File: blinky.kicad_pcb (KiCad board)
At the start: 4 copper layers, 50 x 50 mm, 118 parts, among them J1 Power, J3 Skedd, U1 STM32G030C6Tx, U2 BQ25570

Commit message: Sorting out DRC.
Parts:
- removed R72: 100, Resistor_SMD:R_0402_1005Metric
- removed the TP1 at (114.5, 44.5)
- removed the TP2 at (48.1, 89.2)
- added C20: 100u, Capacitor_SMD:C_1206_3216Metric, F.Cu at (117.5, 122.0)
- added C21: 100u, Capacitor_SMD:C_1206_3216Metric, F.Cu at (110.5, 122.0)
- added C22: 100u, Capacitor_SMD:C_1206_3216Metric, F.Cu at (103.5, 122.0)
- added C23: 100u, Capacitor_SMD:C_1206_3216Metric, F.Cu at (96.5, 122.0)
- added C24: 100u, Capacitor_SMD:C_1206_3216Metric, F.Cu at (89.5, 122.0)
- added C25: 100u, Capacitor_SMD:C_1206_3216Metric, F.Cu at (82.5, 122.0)
- moved TP2 23.7 mm to (93.0, 76.5)
- moved TP1 23.3 mm to (86.0, 79.5)
- moved TP3 20.2 mm to (86.0, 76.5)
- moved R27 5.98 mm to (105.8, 96.0), turned to -90 degrees
- moved R34 1.30 mm to (103.7, 95.2), turned to 90 degrees
- moved R33 1.22 mm to (95.9, 95.8)
- moved R44 1.03 mm to (103.7, 104.8), turned to -90 degrees
- moved R43 1.03 mm to (95.8, 104.3)
- moved C8 0.67 mm to (92.8, 101.2), turned to 90 degrees
- moved C1 0.25 mm to (94.3, 100.0)
- moved R21 0.13 mm to (85.5, 89.5)
- turned R24 to 180 degrees
- turned R45 to 180 degrees
- renumbered J3 to J2, R71 to R10, R73 to R18, R18 to R19, R19 to R20, R74 to R27, TP3 to TP1, TP4 to TP2, TP5 to TP3
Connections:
- J2 pad 1: /d3V3 -> +3V3
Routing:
- net +3V3: track 186.1 -> 273.0 mm, vias 0 -> 6
- net /VBatt: track 69.6 -> 141.6 mm
- net GND: track 16.1 -> 54.6 mm, vias 12 -> 34
- net Net-(D43-K): track 0.00 -> 2.73 mm, vias 0 -> 1
- net Net-(D33-K): track 0.00 -> 2.28 mm, vias 0 -> 1
- net /A15: track 0.00 -> 1.92 mm
- net /Vin: track 9.57 -> 11.5 mm
- net Net-(D44-K): track 0.00 -> 1.92 mm, vias 0 -> 1
- net Net-(D34-K): track 0.00 -> 1.91 mm, vias 0 -> 1
- net /A2: track 2.57 -> 0.75 mm
- net Net-(D66-K): track 0.00 -> 1.57 mm, vias 0 -> 1
- net Net-(D65-K): track 0.00 -> 1.57 mm, vias 0 -> 1
- net Net-(D64-K): track 0.00 -> 1.57 mm, vias 0 -> 1
- net Net-(D63-K): track 0.00 -> 1.57 mm, vias 0 -> 1
- net Net-(D62-K): track 0.00 -> 1.57 mm, vias 0 -> 1
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- added copper zone on B.Cu, net +3V3
- added copper zone on B.Cu, net GND
- added copper zone on In1.Cu, net GND
- added copper zone on In2.Cu, net GND

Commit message: Cap to the max.
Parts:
- added C10: 100u, Capacitor_SMD:C_1206_3216Metric, F.Cu at (78.8, 78.8)
- added C17: 100u, Capacitor_SMD:C_1206_3216Metric, F.Cu at (121.2, 78.8)
- added C22: 100u, Capacitor_SMD:C_1206_3216Metric, F.Cu at (121.2, 121.2)
- added C29: 100u, Capacitor_SMD:C_1206_3216Metric, F.Cu at (78.8, 121.2)
- added C9: 47u, Capacitor_SMD:C_0805_2012Metric, F.Cu at (91.7, 100.0)
- moved J1 1.13 mm to (79.9, 85.5), turned to -90 degrees
- moved C11 1.00 mm to (83.5, 78.0)
- moved C16 1.00 mm to (116.5, 78.0)
- moved C18 1.00 mm to (122.0, 83.5)
- moved C21 1.00 mm to (122.0, 116.5)
- moved C23 1.00 mm to (116.5, 122.0)
- moved C28 1.00 mm to (83.5, 122.0)
- moved C8 0.72 mm to (93.5, 101.7), turned to 180 degrees
- renumbered C10 to C11, C11 to C12, C12 to C13, C13 to C14, C14 to C15, C15 to C16, C16 to C18, C17 to C19, C18 to C20, C19 to C21, C20 to C23, C21 to C24, C22 to C25, C23 to C26, C24 to C27, C25 to C28
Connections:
- U1 pad 4: +3V3 -> Net-(U1-VBAT)
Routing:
- net GND: track 54.6 -> 61.1 mm, vias 34 -> 40
- net /VBatt: track 141.6 -> 147.5 mm
- net Net-(U1-VBAT): track 0.00 -> 3.97 mm
- net /RESET: track 27.1 -> 25.0 mm
- net +3V3: track 273.0 -> 271.4 mm, vias 6 -> 10
- net /Vin: track 11.5 -> 10.5 mm

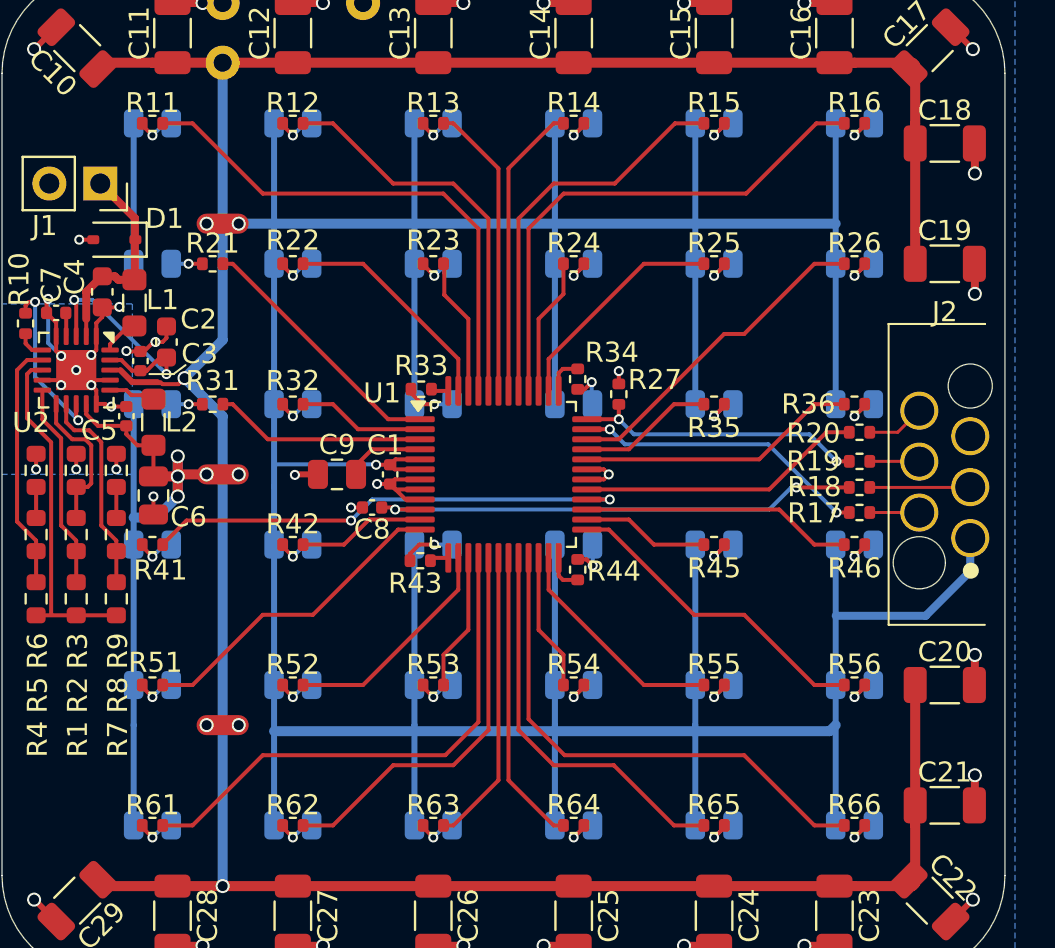
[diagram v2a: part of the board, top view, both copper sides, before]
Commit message: Sort out resistor values.
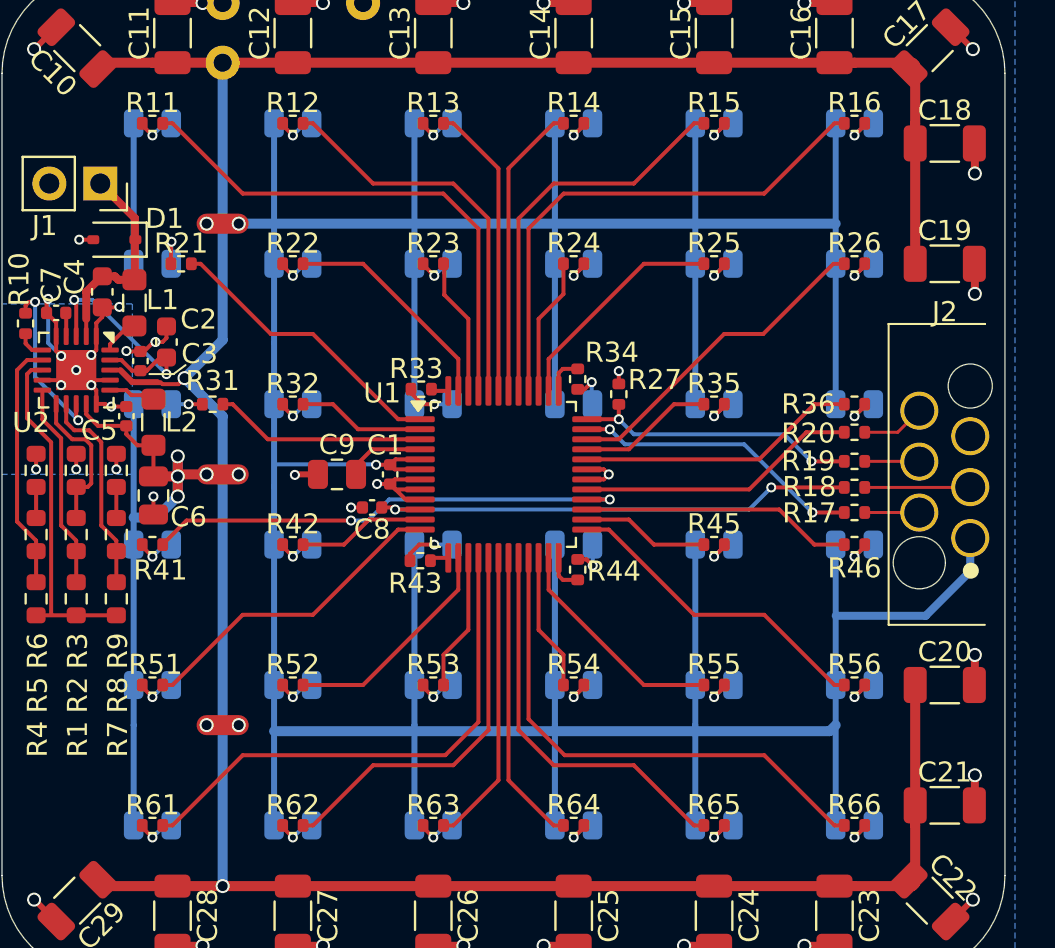
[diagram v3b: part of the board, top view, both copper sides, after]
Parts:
- R1: value 634k -> 1M8
- R10, R27: value 100k -> 10k
- R11, R12, R13, R14, R15, R16, R21, R22, R23, R24, R25, R26, R31, R32, R33, R34, R35, R36, R41, R42, R43, R44, R45, R46, R51, R52, R53, R54, R55, R56, R61, R62, R63, R64, R65, R66: value 100 -> 470
- R2: value 6M2 -> 6M8
- R3: value 3M9 -> 2M2
- R4: value 5M1 -> 6M2
- R5: value 430k -> 330k
- R6: value 3M9 -> 3M
- R7: value 6M8 -> 5M1
- R8: value 330k -> 750k
- R9: value 3M6 -> 2M2
- moved R21 1.57 mm to (83.9, 89.5)
- moved R17 0.25 mm to (117.5, 101.9)
- moved R18 0.25 mm to (117.5, 100.7)
- moved R19 0.25 mm to (117.5, 99.3)
- moved R20 0.25 mm to (117.5, 97.9)
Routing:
- net /C13: track 13.2 -> 14.6 mm
- net Net-(D21-K): track 1.52 -> 2.22 mm

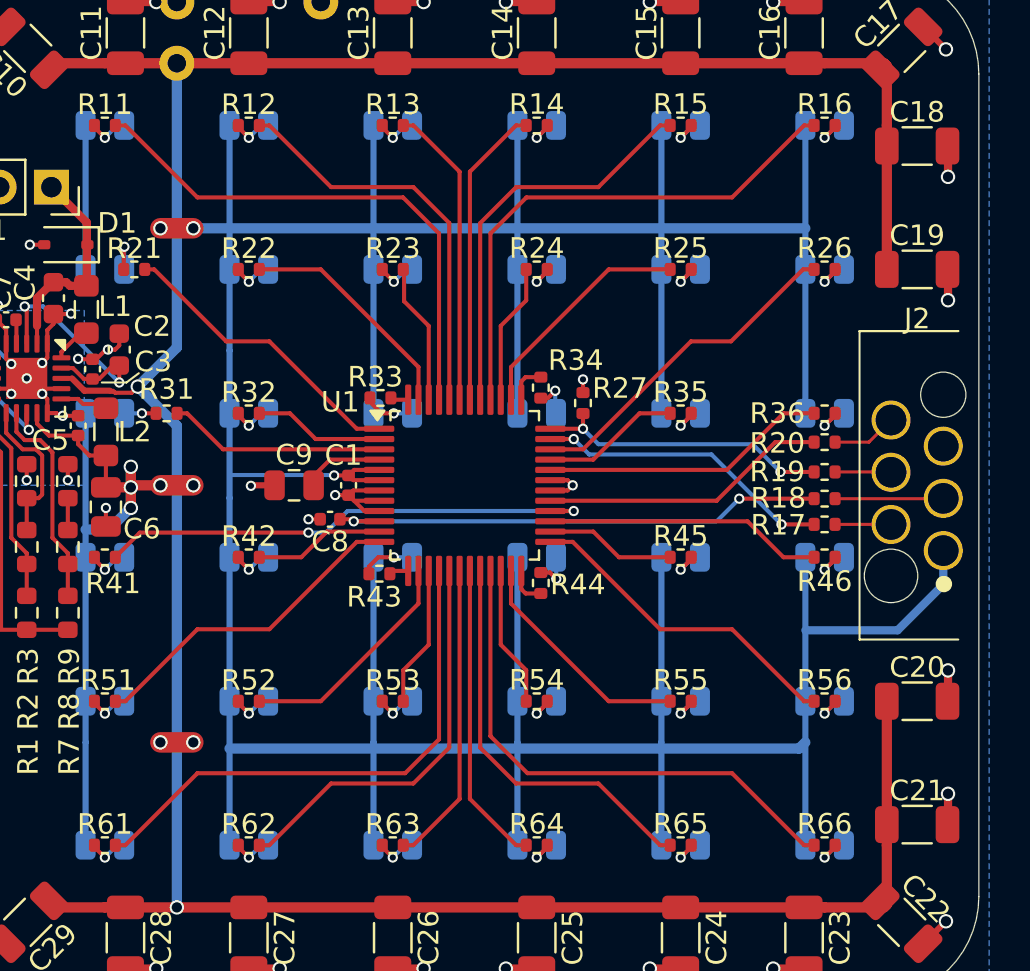
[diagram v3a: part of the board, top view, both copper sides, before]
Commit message: Flip debug connector.
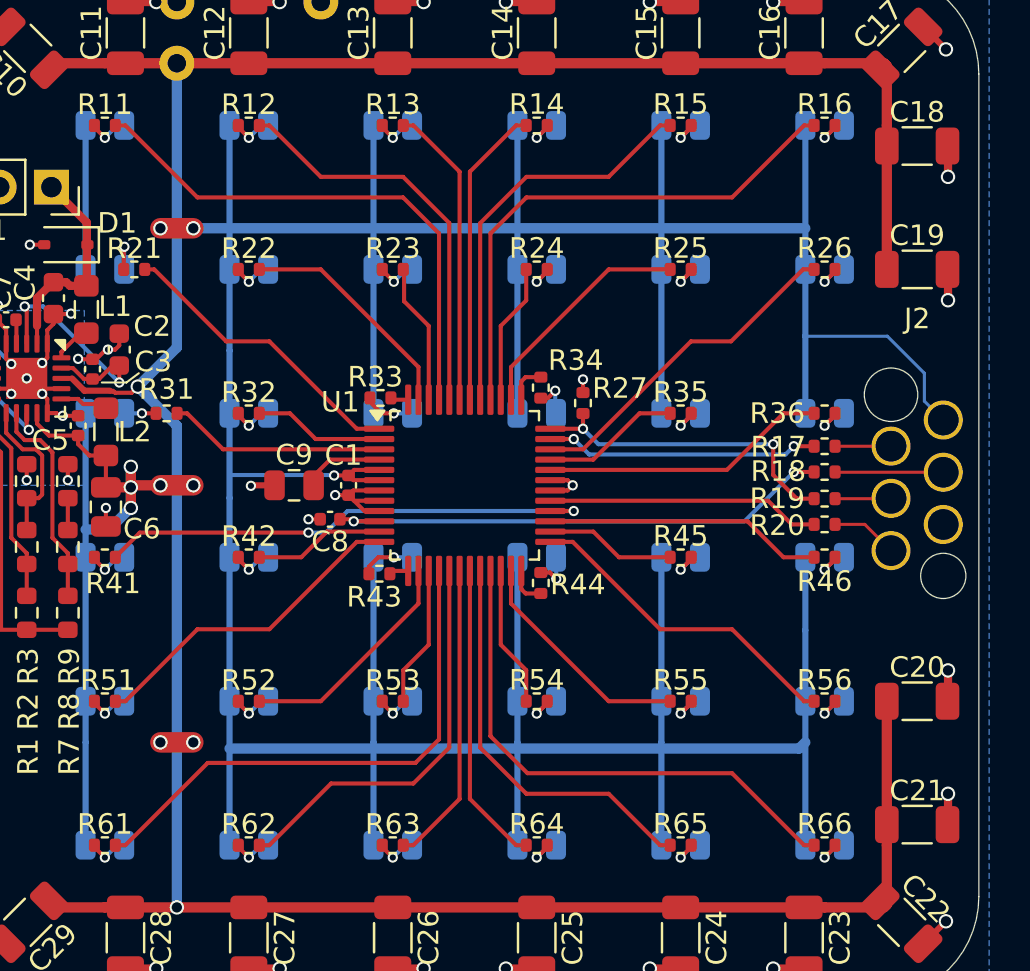
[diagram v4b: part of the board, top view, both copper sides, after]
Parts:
- J2: moved to B.Cu
- moved R20 4.00 mm to (117.5, 101.9)
- moved R17 3.80 mm to (117.5, 98.1)
- moved R18 1.30 mm to (117.5, 99.3)
- moved R19 1.30 mm to (117.5, 100.7)
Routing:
- net /SWCLK: track 14.4 -> 15.9 mm
- net /SWDIO: track 14.5 -> 13.3 mm
- net /SERTX: track 14.0 -> 13.3 mm
- net /RESET: track 24.8 -> 25.3 mm

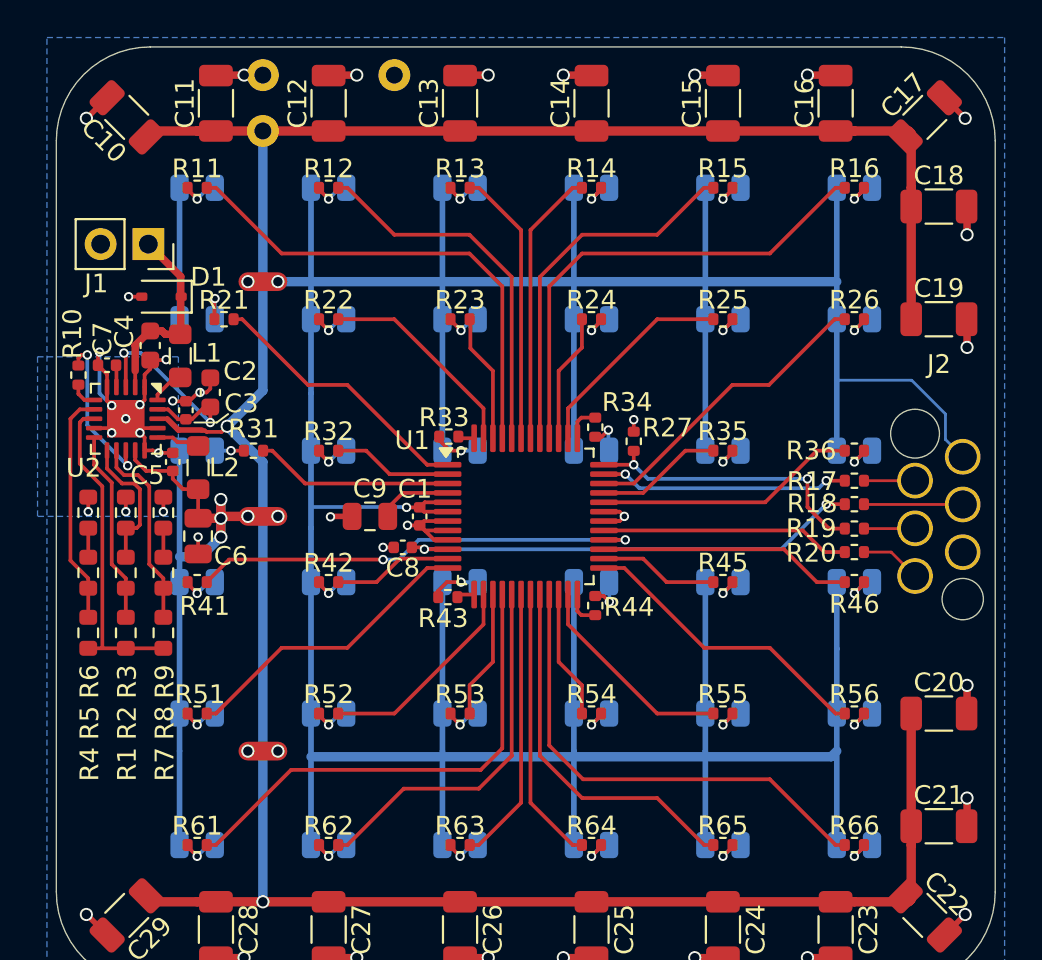
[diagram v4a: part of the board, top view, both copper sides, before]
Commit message: Add room for power connector socket.
Adjust skedd connector foot-print to fit board.
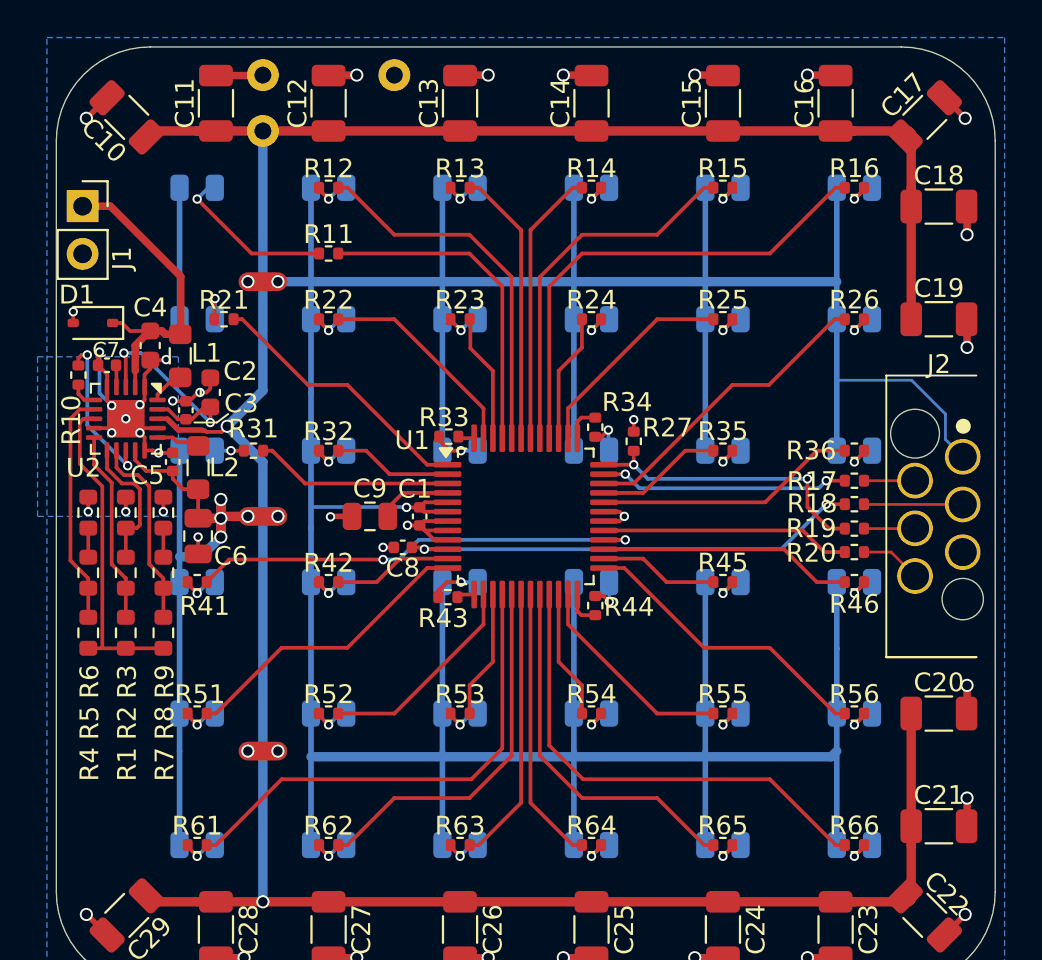
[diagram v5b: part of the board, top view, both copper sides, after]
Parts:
- moved R11 7.83 mm to (89.5, 86.0)
- moved J1 4.04 mm to (76.4, 83.5), turned to 0 degrees
- moved D1 3.91 mm to (77.0, 89.7)
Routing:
- net /B6: track 26.0 -> 17.6 mm
- net Net-(D11-K): track 1.57 -> 8.54 mm
- net /Vin: track 10.5 -> 17.0 mm
- net GND: track 61.1 -> 62.0 mm, vias 40 -> 39

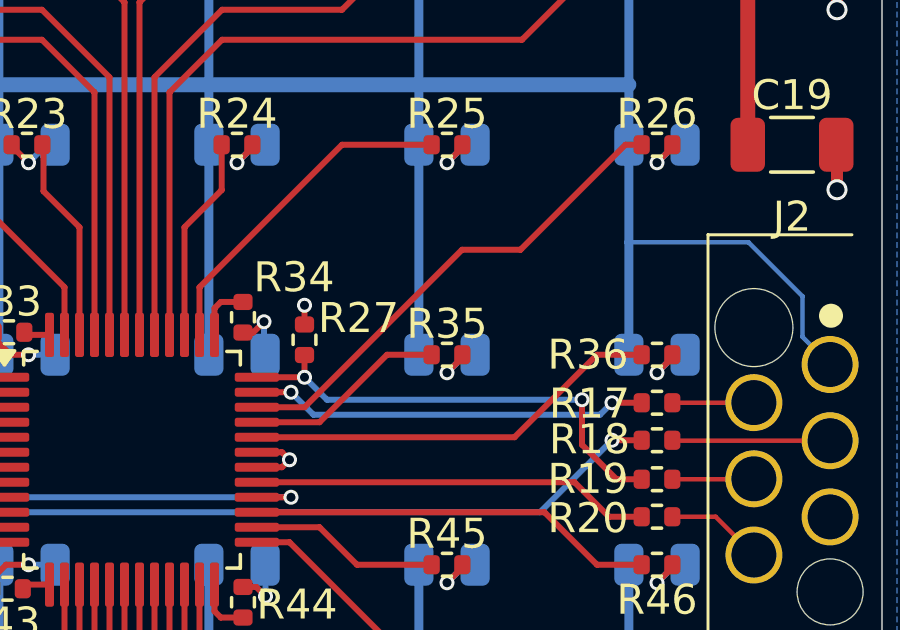
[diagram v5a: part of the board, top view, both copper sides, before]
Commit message: Use 330 ohm resistors.
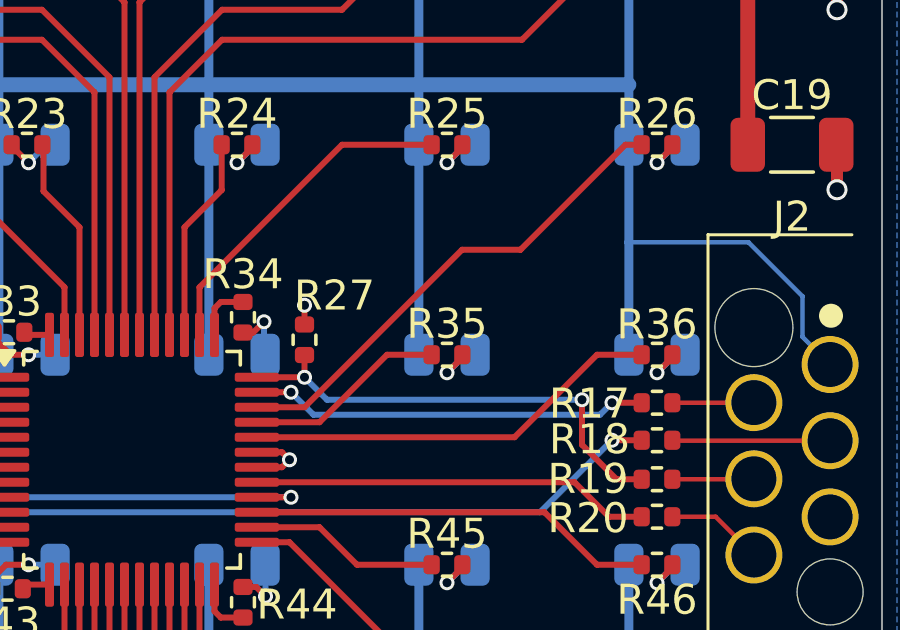
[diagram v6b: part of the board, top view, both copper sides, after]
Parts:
- R11, R12, R13, R14, R15, R16, R21, R22, R23, R24, R25, R26, R31, R32, R33, R34, R35, R36, R41, R42, R43, R44, R45, R46, R51, R52, R53, R54, R55, R56, R61, R62, R63, R64, R65, R66: value 470 -> 330
